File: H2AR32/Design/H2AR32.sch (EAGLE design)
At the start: 57 parts, among them P1 HEXABIT__NO_P1_P5_P6_P7_P12, U1 STM32G0B1CEU6N, U2 INA199B2DCKT, U3 INA199B1DCKT, U4 TEXAS_INSTRUMENTS_REF2033AIDD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, X1 XTALL_CSTCE8M00G52

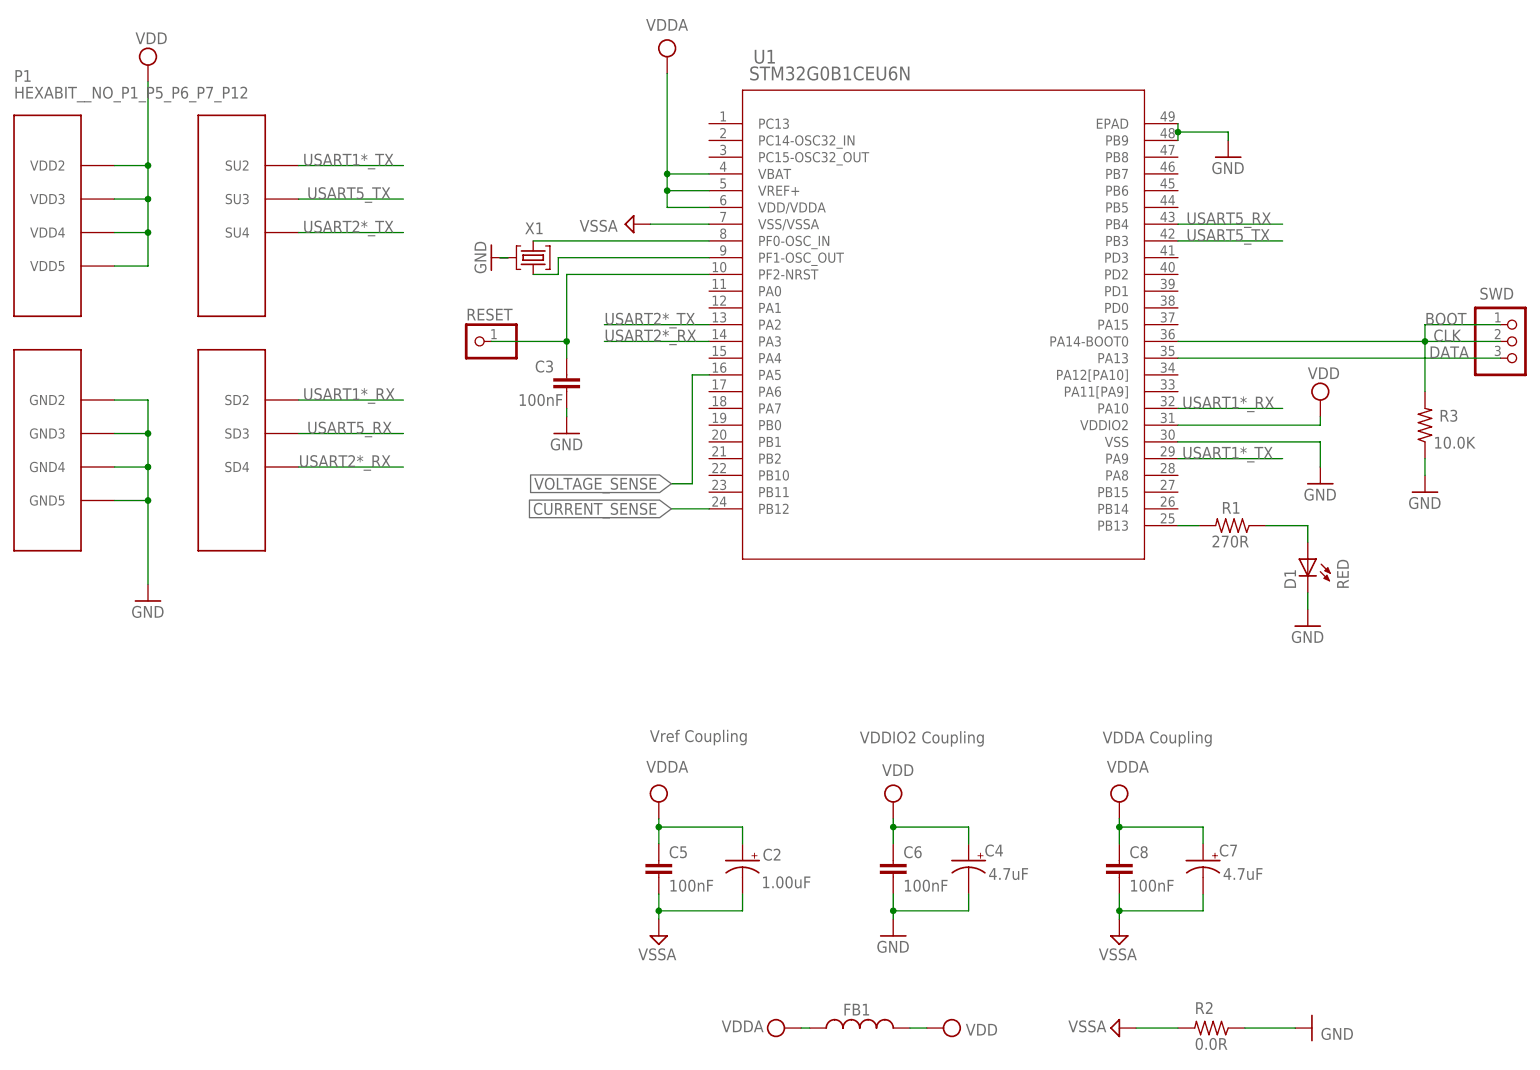
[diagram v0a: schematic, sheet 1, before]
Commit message: -Update the pcb layout design to be based on 4 layers for better performance and improve the analog design
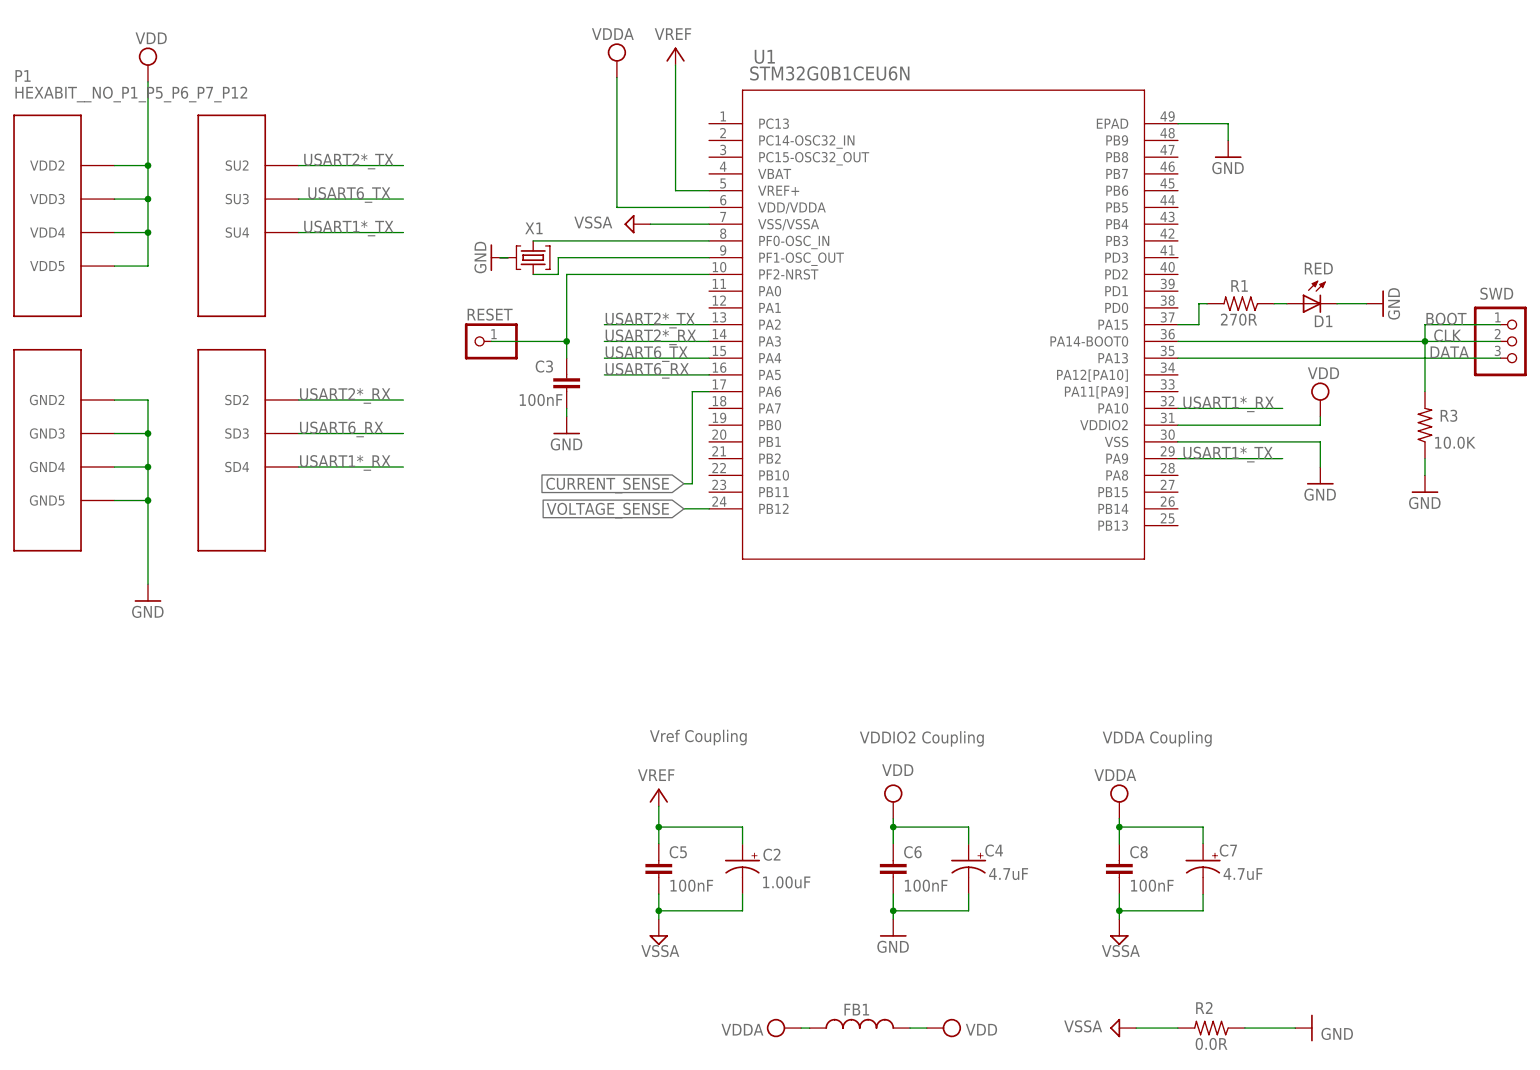
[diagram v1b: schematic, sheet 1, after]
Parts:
- added C20: 100nF, HEXABITZ_RCLS:C-0603
- R10, R14, R16, R8, R9: device HEXABITZ_RCLS:R-0603 -> HEXABITZ_RCLS:R_1206R1206
- U4: MPN (none) -> REF2030AIDDCR
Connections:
- net V_REF renamed VBAIS
- removed net AGND: C1.-, C11.1, C12.2, C13.2, C14.2, C15.2, C17.1, C18.2, C19.2, C2.-, C21.2, C22.2, C23.2, C24.-, C5.2, C7.-, C8.2, C9.-, R2.2, U1.VSS/VSSA, U2.GND, U3.GND, U4.GND
- removed net N$28: R1.2, U1.PB13
- removed net USART5_RX: P1.SD3, U1.PB4
- removed net USART5_TX: P1.SU3, U1.PB3
- removed net VCC: C1.+, C13.1, C14.1, C2.+, C21.1, C24.+, C5.1, C7.+, C8.1, C9.+, FB1.1, R15.2, U1.VBAT, U1.VDD/VDDA, U1.VREF+, U2.V+, U3.V+, U4.VIN
- new net N$1: R1.2, U1.PA15
- new net USART6_RX: P1.SD3, U1.PA5
- new net USART6_TX: P1.SU3, U1.PA4
- new net VDDA: C1.+, C13.1, C14.1, C21.1, C24.+, C7.+, C8.1, C9.+, FB1.1, R15.2, U1.VDD/VDDA, U2.V+, U3.V+, U4.VIN
- new net VREF: C2.+, C20.1, C5.1, U1.VREF+, U4.VREF
- new net VSSA: C1.-, C11.1, C12.2, C13.2, C14.2, C15.2, C17.1, C18.2, C19.2, C2.-, C20.2, C21.2, C22.2, C23.2, C24.-, C5.2, C7.-, C8.2, C9.-, R2.2, U1.VSS/VSSA, U2.GND, U3.GND, U4.GND
- net CURRENT_SENSE: now also U1.PA6; no longer U1.PB12
- net GND: no longer U1.PB9
- net USART1*_RX: now also P1.SD4; no longer P1.SD2
- net USART1*_TX: now also P1.SU4; no longer P1.SU2
- net USART2*_RX: now also P1.SD2; no longer P1.SD4
- net USART2*_TX: now also P1.SU2; no longer P1.SU4
- net VOLTAGE_SENSE: now also U1.PB12; no longer U1.PA5
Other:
- note added: "H2AR3_Backend"
- note added: "VBAIS = 1.50V"
- note added: "VREF = 3.0V"
- note removed: "H2AR3_backend"
- note removed: "V_ref = 1.65V"
- moved on the sheet: C23, D1, R1
